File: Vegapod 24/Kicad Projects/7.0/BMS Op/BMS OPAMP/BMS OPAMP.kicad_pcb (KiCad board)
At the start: 2 copper layers, 85.1 x 85.1 mm, 142 parts, among them J1 CHG/DSCHG CTRL, J2 CHG/DSCHG CTRL CMP (SHORT DAT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, J3 Data IN/OUT, J4 Data IN/OUT, J5 Port Selector, J6 Port Selector, J7 NTC1, J8 NTC2, J9 Balance Connector, Q1 MMBT3906, Q2 MMBT3904, Q3 MMBT3904, Q4 MMBT3904, Q5 MMBT3904, Q6 MMBT3904, Q7 MMBT3904, U1 TLP185, U10 LM324, U11 LM324, U2 TLP185, U3 TLP185, U4 TLP185, U5 TLP185, U6 6N137, U7 6N137, U8 LM78M05_TO252, U9 LM324

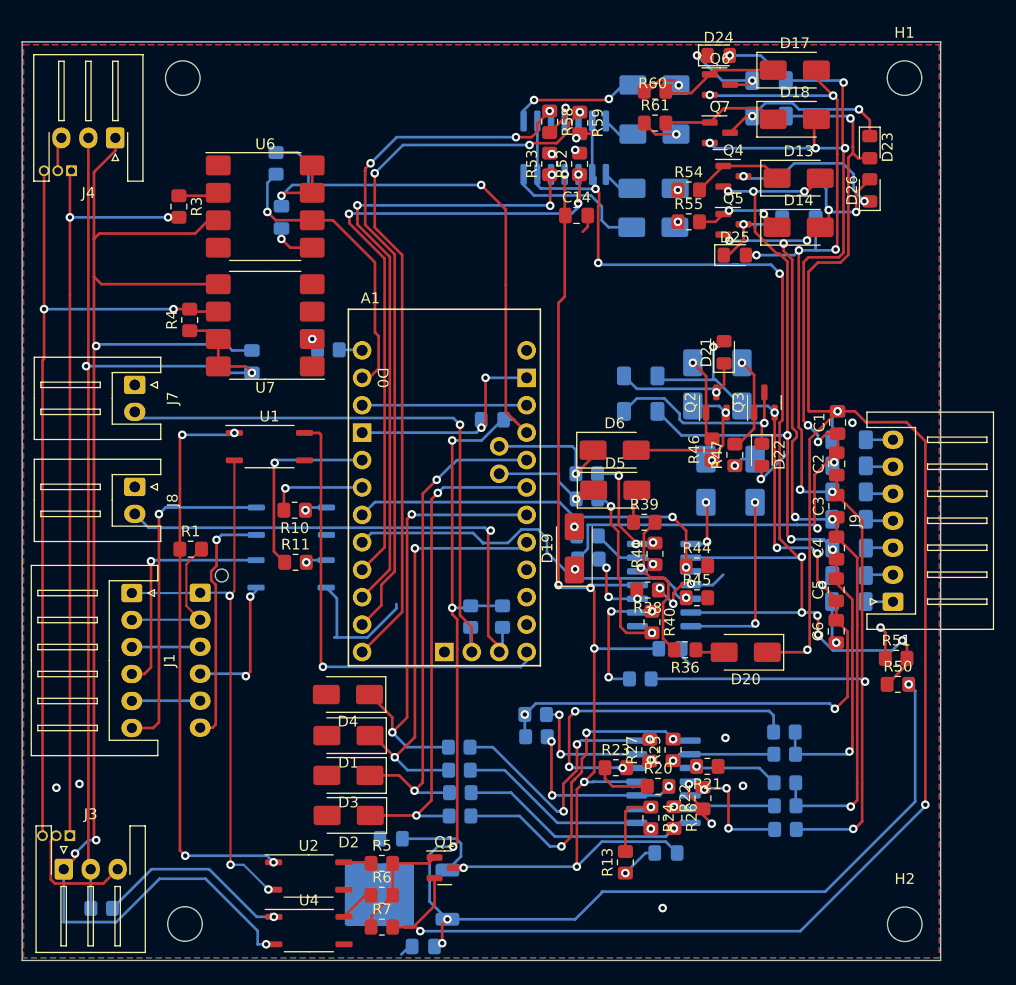
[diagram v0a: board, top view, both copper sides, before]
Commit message: External trigger stm code, OPAMP BMS 1mm via
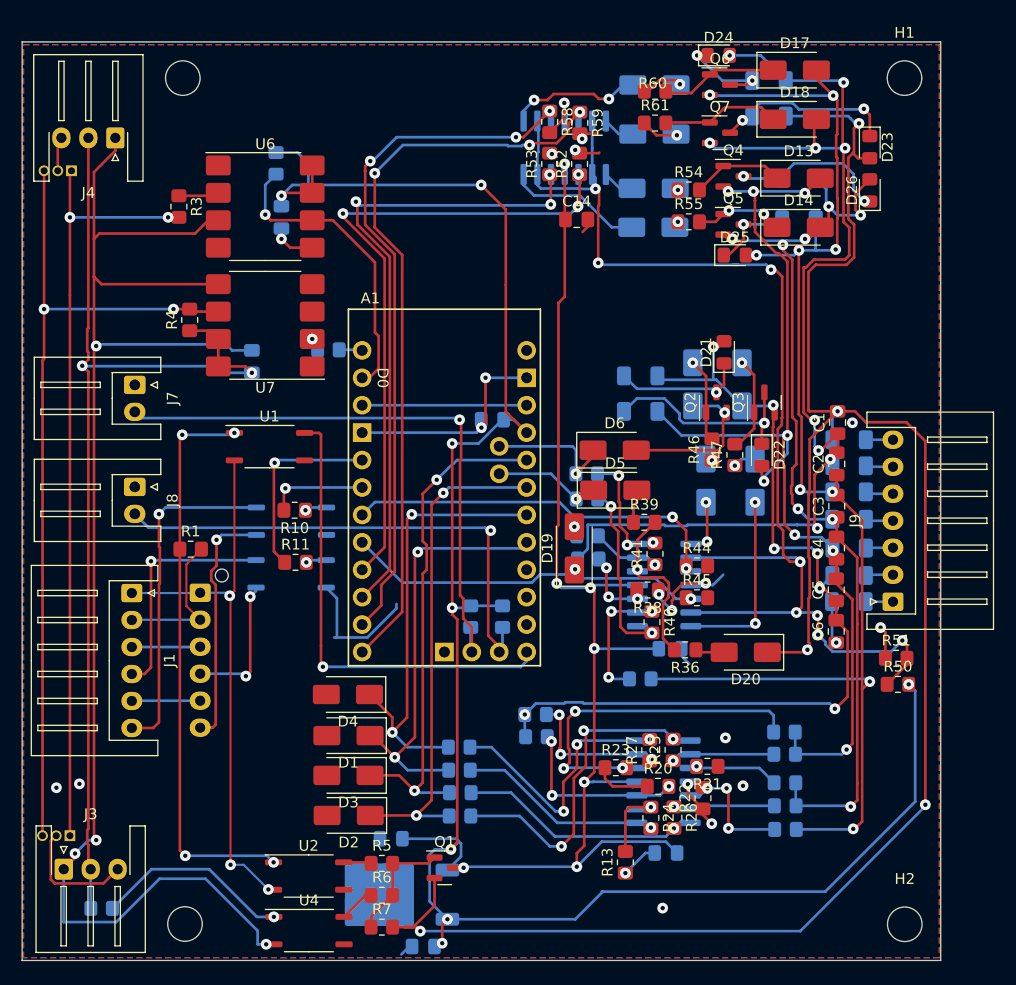
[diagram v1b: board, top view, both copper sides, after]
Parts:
- moved C14 0.37 mm to (73.8, 32.2)
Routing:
- net B0: track 95.7 -> 100.5 mm
- net Net-(U10B-+): track 15.6 -> 18.4 mm
- net D1: track 35.4 -> 33.2 mm
- net POW: track 115.6 -> 117.6 mm
- net B5: track 104.1 -> 106.0 mm
- net B6: track 174.3 -> 176.0 mm
- net B4: track 126.5 -> 128.0 mm
- net B3: track 87.5 -> 88.9 mm
- net B1: track 82.6 -> 84.0 mm
- net DIN_VCC: track 95.9 -> 97.0 mm
- net Net-(U9B-+): track 31.8 -> 32.8 mm
- net Net-(D12-A): track 13.4 -> 12.6 mm
- net Net-(R41-Pad2): track 10.5 -> 11.3 mm
- net D2: track 59.8 -> 60.5 mm
- net Vref: track 113.2 -> 113.9 mm
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
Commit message: Almost complete bms slave
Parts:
- removed U5: TLP185, Package_SO:SOIC-4_4.55x3.7mm_P2.54mm
- added J10: Port Selector, Connector_PinHeader_1.27mm:PinHeader_1x03_P1.27mm_Vertical, F.Cu at (44.8, 76.5)
- added J11: Port Selector, Connector_PinHeader_1.27mm:PinHeader_1x03_P1.27mm_Vertical, F.Cu at (42.3, 73.1)
- added J18: Conn_02x06_Odd_Even, Connector_PinSocket_2.00mm:PinSocket_2x06_P2.00mm_Vertical, F.Cu at (105.7, 35.2)
- added Q10: MMBT3904/AM2304/AO3400, Package_TO_SOT_SMD:SOT-23, B.Cu at (64.6, 41.2)
- added Q8: MMBT3904/AM2304/AO3400, Package_TO_SOT_SMD:SOT-23, B.Cu at (64.6, 33.8)
- added Q9: MMBT3904/AM2304/AO3400, Package_TO_SOT_SMD:SOT-23, B.Cu at (64.6, 37.4)
- added R64: 47K, Resistor_SMD:R_0805_2012Metric_Pad1.20x1.40mm_HandSolder, B.Cu at (92.0, 44.9)
- added R65: 47K, Resistor_SMD:R_0805_2012Metric_Pad1.20x1.40mm_HandSolder, F.Cu at (92.2, 25.7)
- added R66: 47K, Resistor_SMD:R_0805_2012Metric_Pad1.20x1.40mm_HandSolder, F.Cu at (92.4, 20.2)
- added R67: 47K, Resistor_SMD:R_0805_2012Metric_Pad1.20x1.40mm_HandSolder, F.Cu at (93.3, 36.8)
- added R68: 47K, Resistor_SMD:R_0805_2012Metric_Pad1.20x1.40mm_HandSolder, F.Cu at (93.1, 31.2)
- added R69: 470, Resistor_SMD:R_0805_2012Metric_Pad1.20x1.40mm_HandSolder, F.Cu at (84.5, 42.8)
- added R70: 470, Resistor_SMD:R_0805_2012Metric_Pad1.20x1.40mm_HandSolder, F.Cu at (91.0, 58.4)
- added R71: 470, Resistor_SMD:R_0805_2012Metric_Pad1.20x1.40mm_HandSolder, F.Cu at (104.4, 25.6)
- added R72: 470, Resistor_SMD:R_0805_2012Metric_Pad1.20x1.40mm_HandSolder, F.Cu at (86.8, 16.9)
- added R73: 470, Resistor_SMD:R_0805_2012Metric_Pad1.20x1.40mm_HandSolder, F.Cu at (88.5, 37.6)
- added R74: 470, Resistor_SMD:R_0805_2012Metric_Pad1.20x1.40mm_HandSolder, F.Cu at (104.5, 29.5)
- added R75: 33, Resistor_SMD:R_1206_3216Metric_Pad1.30x1.75mm_HandSolder, F.Cu at (79.8, 46.6)
- added R76: 33, Resistor_SMD:R_1206_3216Metric_Pad1.30x1.75mm_HandSolder, F.Cu at (79.8, 50.0)
- added R77: 33, Resistor_SMD:R_1206_3216Metric_Pad1.30x1.75mm_HandSolder, B.Cu at (91.5, 25.1)
- added R78: 33, Resistor_SMD:R_1206_3216Metric_Pad1.30x1.75mm_HandSolder, B.Cu at (91.7, 17.0)
- added R79: 33, Resistor_SMD:R_1206_3216Metric_Pad1.30x1.75mm_HandSolder, B.Cu at (94.5, 34.6)
- added R80: 33, Resistor_SMD:R_1206_3216Metric_Pad1.30x1.75mm_HandSolder, B.Cu at (94.5, 29.9)
- added R81: 4.7k, Resistor_SMD:R_0805_2012Metric_Pad1.20x1.40mm_HandSolder, F.Cu at (66.9, 75.9)
- added R82: 4.7k, Resistor_SMD:R_0805_2012Metric_Pad1.20x1.40mm_HandSolder, F.Cu at (64.8, 75.9)
- added R83: 470, Resistor_SMD:R_0805_2012Metric_Pad1.20x1.40mm_HandSolder, F.Cu at (62.0, 32.9)
- added R84: 470, Resistor_SMD:R_0805_2012Metric_Pad1.20x1.40mm_HandSolder, F.Cu at (62.0, 34.9)
- added R85: 470, Resistor_SMD:R_0805_2012Metric_Pad1.20x1.40mm_HandSolder, F.Cu at (62.0, 36.9)
- added U12: PC817, Package_SO:SSO-4_6.7x5.1mm_P2.54mm_Clearance8mm, F.Cu at (49.0, 97.9)
- D10, D13, D14, D17, D18, D9: value 1n4007 -> 12V Z
- D11, D12, D15, D16, D7, D8: value 1n4007 -> M7
- D19, D20: value 5.1V Z -> Short It Out
- J2: footprint Connector_JST:JST_XH_B6B-XH-AM_1x06_P2.50mm_Vertical -> Connector_PinHeader_2.54mm:PinHeader_1x06_P2.54mm_Vertical; moved to F.Cu
- J3: footprint Connector_JST:JST_XH_S3B-XH-A-1_1x03_P2.50mm_Horizontal -> Connector_JST:JST_XH_B3B-XH-A_1x03_P2.50mm_Vertical
- J7: value NTC1 -> Port Selector; footprint Connector_JST:JST_XH_S2B-XH-A_1x02_P2.50mm_Horizontal -> Connector_PinHeader_1.27mm:PinHeader_1x03_P1.27mm_Vertical
- J8: value NTC2 -> Port Selector; footprint Connector_JST:JST_XH_S2B-XH-A_1x02_P2.50mm_Horizontal -> Connector_PinHeader_1.27mm:PinHeader_1x03_P1.27mm_Vertical
- J9: footprint Connector_JST:JST_XH_S7B-XH-A_1x07_P2.50mm_Horizontal -> Connector_PinSocket_2.54mm:PinSocket_1x07_P2.54mm_Vertical
- Q1: value MMBT3906 -> MMBT3906/FDN358P
- Q2, Q3, Q4, Q5, Q6, Q7: value MMBT3904 -> MMBT3904/AM2304/AO3400
- R1: value 330 -> 470
- R12, R14, R15, R16, R17, R18, R19, R21, R22, R23, R25, R26, R27, R34, R35, R36, R37, R38, R39, R40, R41, R44, R45, R52, R53, R58, R59: value 10k -> 47K
- R13, R20, R24: value 10k -> 47k
- R28, R29, R30, R31, R42, R43: value 10k -> 470
- R32: value 1k -> 470; moved to F.Cu
- R33: value 1k -> 47K
- R46, R47, R50, R51, R54, R55, R60: value 1k -> 470
- R61: value 1k -> SHORT OUT
- U1, U2, U3: value TLP185 -> PC817; footprint Package_SO:SOIC-4_4.55x3.7mm_P2.54mm -> Package_SO:SSO-4_6.7x5.1mm_P2.54mm_Clearance8mm
- U4: value TLP185 -> PC817; footprint Package_SO:SOIC-4_4.55x3.7mm_P2.54mm -> Package_SO:SSO-4_6.7x5.1mm_P2.54mm_Clearance8mm; moved to B.Cu
- moved U4 30.5 mm to (46.3, 67.7), turned to 180 degrees
- moved R33 29.3 mm to (81.5, 43.5)
- moved R32 27.3 mm to (38.1, 60.3), turned to 0 degrees
- moved J7 13.5 mm to (30.1, 60.7), turned to 180 degrees
- moved R2 9.00 mm to (36.8, 90.3)
- moved J3 4.78 mm to (31.1, 92.2), turned to 180 degrees
- moved R7 4.57 mm to (59.6, 95.2)
- moved D24 4.10 mm to (82.9, 16.9)
- moved R6 2.50 mm to (56.8, 92.5)
- moved U1 1.79 mm to (43.6, 53.2)
- moved R5 1.76 mm to (56.8, 90.4)
- moved D4 1.57 mm to (54.2, 76.3)
- moved D1 1.52 mm to (54.2, 80.0)
- moved D3 1.50 mm to (54.2, 83.7)
- moved D2 1.47 mm to (54.2, 87.4)
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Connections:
- A1 pad D11: unconnected-(A1-D11_MOSI-PadD11) -> DTEMP1
- A1 pad D12: unconnected-(A1-D12_MISO-PadD12) -> DTEMP2
- A1 pad D13: unconnected-(A1-D13_SCK-PadD13) -> DTEMP3
- D21 pad 2: B1 -> Net-(D21-A)
- D22 pad 2: B2 -> Net-(D22-A)
- D23 pad 2: B6 -> Net-(D23-A)
- D24 pad 2: B5 -> Net-(D24-A)
- D25 pad 2: B4 -> Net-(D25-A)
- D26 pad 2: B3 -> Net-(D26-A)
- J7 pad 1: B0 -> Net-(J7-Pin_1)
- J7 pad 2: A6 -> Net-(J1-Pin_6)
- J8 pad 1: B0 -> Net-(J7-Pin_1)
- J8 pad 2: A7 -> Net-(J2-Pin_6)
- R32 pad 1: 5V -> Net-(R32-Pad1)
- R32 pad 2: A6 -> CHGDT+
- R33 pad 1: 5V -> B0
- R33 pad 2: A7 -> Net-(D9-K)
- U1 pad 1: Net-(R1-Pad1) -> Net-(R32-Pad1)
- U1 pad 3: CHGDT- -> B0
- U1 pad 4: B0 -> DCHG
- U2 pad 3: CHGDT- -> B0
- U2 pad 4: B0 -> Net-(R5-Pad1)
- U3 pad 3: B0 -> Net-(J7-Pin_1)
- U3 pad 4: Net-(J2-Pin_6) -> Net-(J7-Pin_3)
- U4 pad 1: Net-(R2-Pad1) -> Net-(R11-Pad2)
- U4 pad 3: DIN_GND -> Net-(J10-Pin_1)
- U4 pad 4: B0 -> Net-(J10-Pin_3)
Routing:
- net DTEMP1: track 0.00 -> 47.9 mm, vias 0 -> 1
- net NTC_GND1: track 0.00 -> 46.6 mm
- net A7: track 47.8 -> 92.8 mm, vias 1 -> 3
- net NTC_GND3: track 0.00 -> 44.3 mm
- net DTEMP2: track 0.00 -> 44.0 mm, vias 0 -> 1
- net NTC_GND2: track 0.00 -> 42.8 mm
- net DTEMP3: track 0.00 -> 41.2 mm, vias 0 -> 1
- net A6: track 54.8 -> 93.9 mm, vias 1 -> 3
- net B0: track 100.5 -> 122.3 mm, vias 22 -> 24
- net Net-(R1-Pad1): track 52.6 -> 34.2 mm, vias 4 -> 2
- net DIN_GND: track 138.3 -> 122.2 mm, vias 4 -> 2
- net Net-(J7-Pin_1): track 0.00 -> 16.0 mm, vias 0 -> 2
- net Net-(J7-Pin_3): track 0.00 -> 15.9 mm, vias 0 -> 2
- net Net-(J10-Pin_3): track 0.00 -> 12.9 mm
- net B4: track 128.0 -> 138.0 mm, vias 9 -> 8
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- added copper zone on B.Cu, net DIN_GND
- added copper zone on F.Cu, net DIN_GND
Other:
- board text added: "."
- board text added: "0S"
- board text added: "1S"
- board text added: "2S"
- board text added: "3S"
- board text added: "4S"
- board text added: "5S"
- board text added: "6S"
- board text added: "Bottom Board"
- board text added: "DIN"
- board text added: "DOUT"
- board text added: "NTCs"
- board text added: "T1"
- board text added: "T2"
- board text added: "T3"
- board text added: "T4"
- board text added: "T5"
- board text added: "T6"
- board text added: "TOP Board"
- board text added: "Top Board"

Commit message: Almost complete bms slave
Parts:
- added J12: FTDI, Connector_PinSocket_2.54mm:PinSocket_1x06_P2.54mm_Horizontal, F.Cu at (65.5, 26.4)
- added R86: 47K, Resistor_SMD:R_0805_2012Metric_Pad1.20x1.40mm_HandSolder, F.Cu at (97.2, 79.5)
- added R87: 47k, Resistor_SMD:R_0805_2012Metric_Pad1.20x1.40mm_HandSolder, F.Cu at (97.7, 83.5)
- added R88: 47k, Resistor_SMD:R_0805_2012Metric_Pad1.20x1.40mm_HandSolder, F.Cu at (95.5, 83.5)
- added R89: 47k, Resistor_SMD:R_0805_2012Metric_Pad1.20x1.40mm_HandSolder, F.Cu at (93.4, 83.5)
- added R90: 47k, Resistor_SMD:R_0805_2012Metric_Pad1.20x1.40mm_HandSolder, F.Cu at (97.9, 87.8)
- added R91: 47k, Resistor_SMD:R_0805_2012Metric_Pad1.20x1.40mm_HandSolder, F.Cu at (93.9, 87.8)
- added R92: 47k, Resistor_SMD:R_0805_2012Metric_Pad1.20x1.40mm_HandSolder, F.Cu at (91.9, 87.8)
- added R93: 47k, Resistor_SMD:R_0805_2012Metric_Pad1.20x1.40mm_HandSolder, F.Cu at (89.9, 87.8)
- added R94: 47k, Resistor_SMD:R_0805_2012Metric_Pad1.20x1.40mm_HandSolder, F.Cu at (87.9, 87.8)
- added R95: 47k, Resistor_SMD:R_0805_2012Metric_Pad1.20x1.40mm_HandSolder, F.Cu at (95.9, 87.8)
- added R96: 4.7K, Resistor_SMD:R_0805_2012Metric_Pad1.20x1.40mm_HandSolder, F.Cu at (100.4, 54.9)
- added R97: 3.1k, Resistor_SMD:R_0805_2012Metric_Pad1.20x1.40mm_HandSolder, F.Cu at (100.4, 51.0)
- moved J5 2.42 mm to (27.0, 30.1)
- moved J6 1.58 mm to (26.9, 87.7)
- moved R8 1.04 mm to (47.0, 26.7)
- moved C10 0.70 mm to (47.2, 32.0)
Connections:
- net Net-(A1-RESET-PadRST1) renamed RST
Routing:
- net RST: track 15.2 -> 39.9 mm
- net B3: track 93.4 -> 114.1 mm
- net DTX: track 2.15 -> 22.7 mm
- net B4: track 138.0 -> 154.2 mm
- net DRX: track 26.5 -> 42.3 mm, vias 1 -> 5
- net B0: track 122.3 -> 136.0 mm, vias 24 -> 21
- net 5V: track 183.6 -> 196.0 mm
- net B2: track 101.2 -> 109.3 mm
- net B5: track 111.6 -> 118.4 mm
- net DOUT: track 77.9 -> 73.9 mm
- net DIN: track 71.7 -> 67.7 mm
- net Net-(J4-Pin_3): track 3.19 -> 6.11 mm
- net Net-(R27-Pad2): track 24.8 -> 27.6 mm
- net Net-(U9D--): track 9.53 -> 11.6 mm
- net Net-(U9D-+): track 12.7 -> 14.5 mm, vias 3 -> 2
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
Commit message: Almost complete bms slave
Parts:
- R75, R76: moved to B.Cu
- moved R75 4.14 mm to (77.9, 42.9)
- moved R76 2.80 mm to (77.9, 47.9), turned to 0 degrees
- moved R48 2.40 mm to (77.9, 45.2)
- moved R49 1.89 mm to (77.9, 50.2), turned to 0 degrees
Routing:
- net B2: track 109.3 -> 114.7 mm, vias 6 -> 5
- net Net-(D22-K): track 25.1 -> 19.9 mm, vias 2 -> 1
- net B1: track 95.3 -> 98.5 mm, vias 7 -> 6
- net Net-(D21-K): track 14.1 -> 17.0 mm, vias 2 -> 1

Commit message: BMS PCB
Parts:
- D10, D13, D14, D17, D18, D9: value 12V Z -> 5V Z
